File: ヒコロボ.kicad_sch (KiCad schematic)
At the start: 16 parts, among them U1 R3106GF, U2 4053, U3 4053, U5 R3106FG_IF

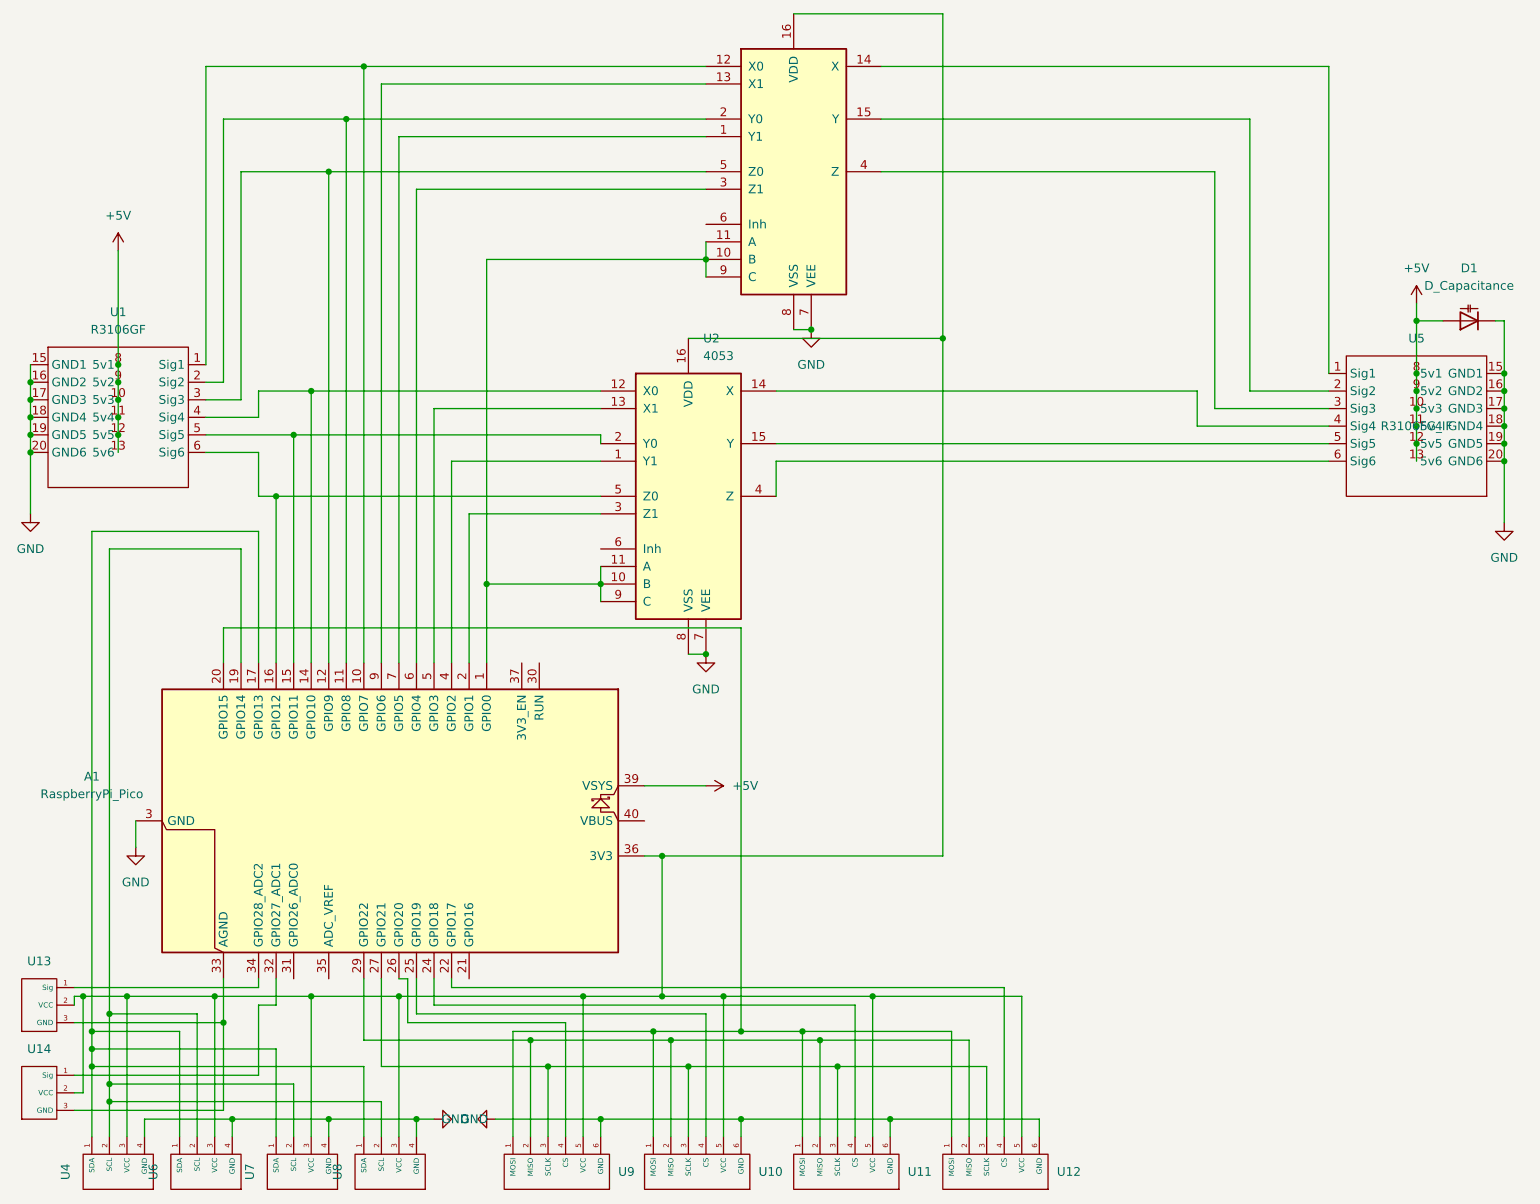
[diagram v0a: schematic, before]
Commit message: 基板回路を刷新
受信機をR3008SBに変更、Seeed XIAO追加、ラズパイ横に汎用ピン追加、各センサ用インターフェース追加
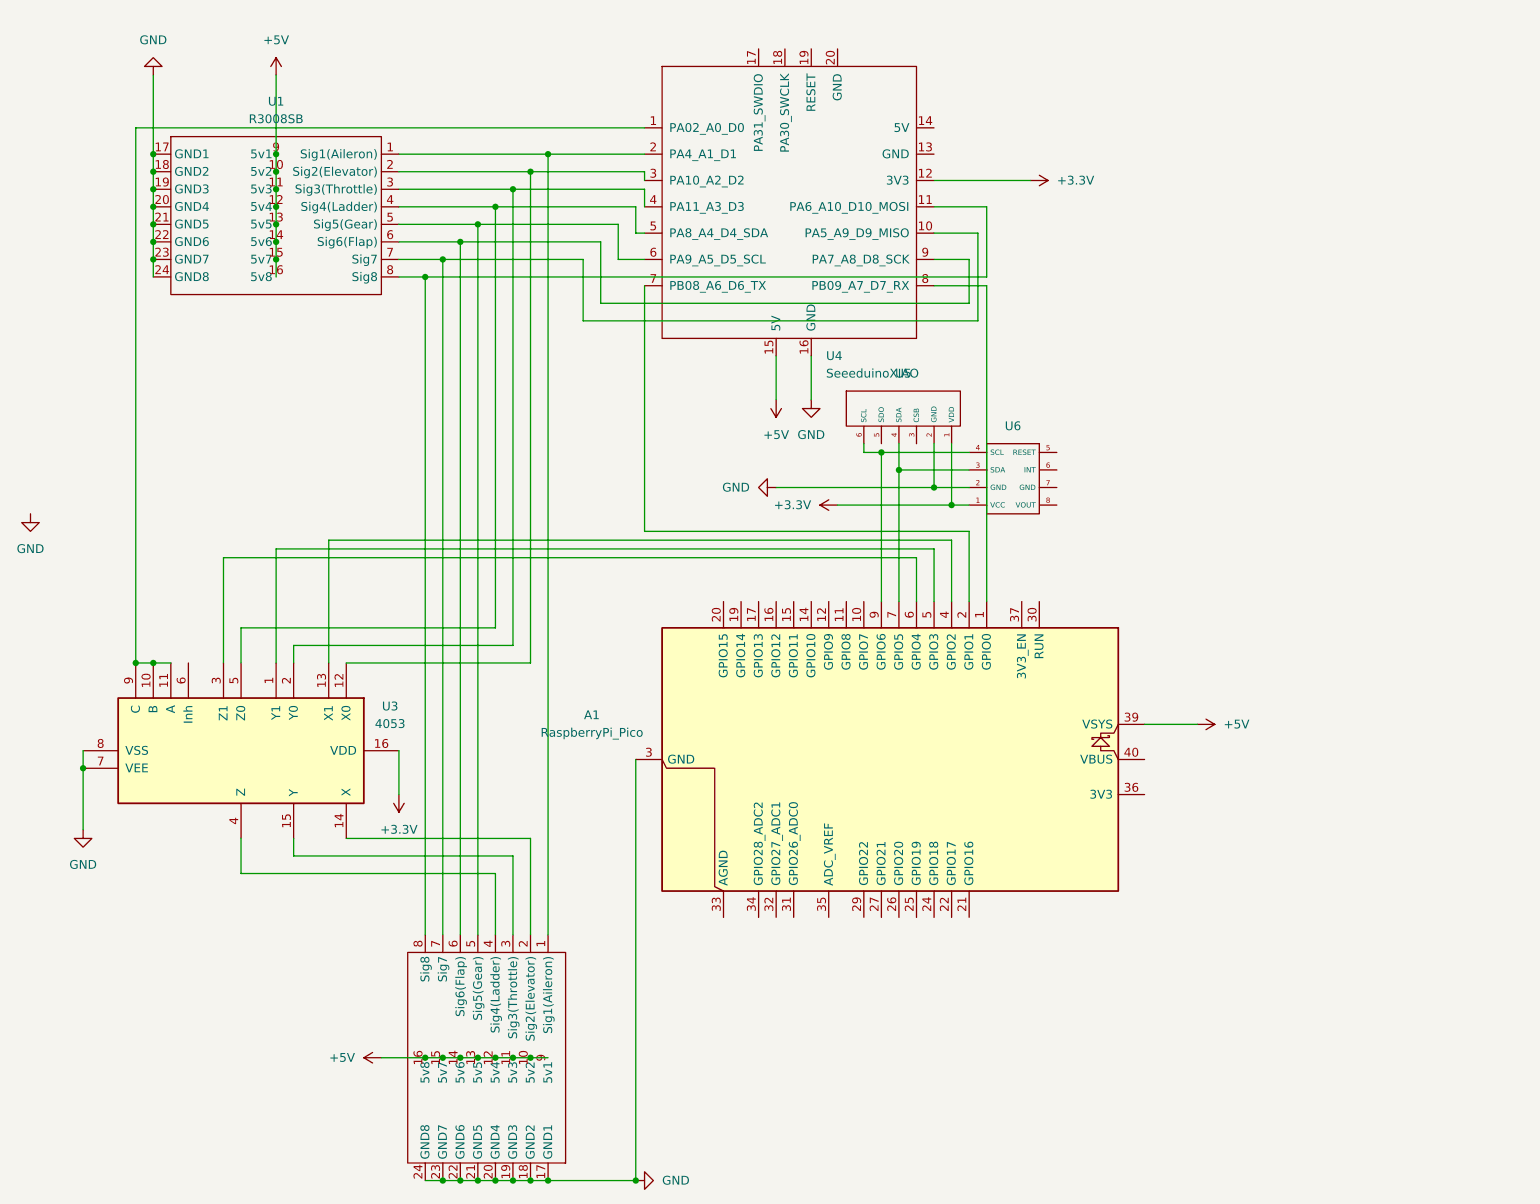
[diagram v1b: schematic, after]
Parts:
- removed D1: D_Capacitance, Capacitor_SMD:CP_Elec_8x10.5, symbol Device:D_Capacitance
- removed U1: R3106GF, Library:R3106FG, symbol My_Library:R3106GF
- removed U10, U11, U12, U9: (no value), Library:Sensor_SPI_IF, symbol My_Library:Sensor_SPI_IF
- removed U13, U14: (no value), Library:Sensor_Analog_IF, symbol My_Library:Sensor_Analog_IF
- removed U2: 4053, Library:DIP794W45P254L1969H508Q16, symbol 4xxx:4053
- removed U4, U6, U7, U8: (no value), Library:Sensor_I2C_IF, symbol My_Library:Sensor_IF
- removed U5: R3106FG_IF, Library:R3106FG, symbol My_Library:R3106GF_IF
- added U1: R3008SB, Library:R3008SB, symbol My_Library:R3008SB
- added U2: (no value), Library:R3008SB, symbol My_Library:R3008SB_IF
- added U4: SeeeduinoXIAO, Library:Seeeduino XIAO-MOUDLE14P-2.54-21X17.8MM, symbol My_Library:SeeeduinoXIAO
- added U5: (no value), Library:BMO280_IF, symbol My_Library:BME280_IF
- added U6: (no value), Library:BNO055_IF, symbol My_Library:BNE055_IF
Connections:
- net +5V: now also U1.10 (5v2), U1.11 (5v3), U1.12 (5v4), U1.13 (5v5), U1.14 (5v6), U1.15 (5v7), U1.16 (5v8), U1.9 (5v1), U2.10 (5v2), U2.11 (5v3), U2.12 (5v4), U2.13 (5v5), U2.14 (5v6), U2.15 (5v7), U2.16 (5v8), U2.9 (5v1), U4.15 (5V)
- net GND: now also U1.17 (GND1), U1.18 (GND2), U1.19 (GND3), U1.20 (GND4), U1.21 (GND5), U1.22 (GND6), U1.23 (GND7), U1.24 (GND8), U2.17 (GND1), U2.18 (GND2), U2.19 (GND3), U2.20 (GND4), U2.21 (GND5), U2.22 (GND6), U2.23 (GND7), U2.24 (GND8), U4.16 (GND), U5.2 (GND), U6.2 (GND)
- net at A1.7 (GPIO5): now also U5.4 (SDA), U6.3 (SDA); no longer U3.1 (Y1)
- net at U3.10 (B), U3.11 (A), U3.9 (C): now also U4.1 (PA02_A0_D0); no longer A1.1 (GPIO0)
- net at A1.10 (GPIO7): no longer U3.12 (X0)
- net at A1.9 (GPIO6): now also U5.6 (SCL), U6.4 (SCL); no longer U3.13 (X1)
- net at U3.14 (X): now also U2.2 (Sig2(Elevator))
- net at U3.15 (Y): now also U2.3 (Sig3(Throttle))
- net at A1.36 (3V3): no longer U3.16 (VDD)
- net at A1.11 (GPIO8): no longer U3.2 (Y0)
- net at U3.4 (Z): now also U2.4 (Sig4(Ladder))
- net at A1.12 (GPIO9): no longer U3.5 (Z0)
- net at A1.4 (GPIO2): now also U3.13 (X1)
- net at A1.5 (GPIO3): now also U3.1 (Y1)
- net at A1.2 (GPIO1): now also U4.7 (PB08_A6_D6_TX)
- new net: A1.1 (GPIO0), U4.8 (PB09_A7_D7_RX)
- new net: U1.1 (Sig1(Aileron)), U2.1 (Sig1(Aileron)), U4.2 (PA4_A1_D1)
- new net: U1.2 (Sig2(Elevator)), U3.12 (X0), U4.3 (PA10_A2_D2)
- new net: U1.3 (Sig3(Throttle)), U3.2 (Y0), U4.4 (PA11_A3_D3)
- new net: U1.4 (Sig4(Ladder)), U3.5 (Z0), U4.5 (PA8_A4_D4_SDA)
- new net: U1.5 (Sig5(Gear)), U2.5 (Sig5(Gear)), U4.6 (PA9_A5_D5_SCL)
- new net: U1.6 (Sig6(Flap)), U2.6 (Sig6(Flap)), U4.9 (PA7_A8_D8_SCK)
- new net: U1.7 (Sig7), U2.7 (Sig7), U4.10 (PA5_A9_D9_MISO)
- new net: U1.8 (Sig8), U2.8 (Sig8), U4.11 (PA6_A10_D10_MOSI)
- new net +3.3V: U3.16 (VDD), U4.12 (3V3), U5.1 (VDD), U6.1 (VCC)
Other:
- moved on the sheet: A1

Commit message: 確認お願いします。デザインルールチェッカーはエラーなしで通過してます。
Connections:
- net at U5.4 (SDA), U6.3 (SDA): now also A1.9 (GPIO6); no longer A1.7 (GPIO5)
- net at U5.6 (SCL), U6.4 (SCL): now also A1.10 (GPIO7); no longer A1.9 (GPIO6)
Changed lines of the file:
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@@
+	)
+	(junction
+		(at 139.7 82.55)
+		(diameter 0)
+		(color 0 0 0 0)
+	)
+	(junction
+		(at 134.62 80.01)
+		(diameter 0)
+		(color 0 0 0 0)
 	)
 	(junction
@@
 	)
 	(junction
-		(at 139.7 82.55)
-		(diameter 0)
-		(color 0 0 0 0)
-	)
-	(junction
 		(at 31.75 44.45)
 		(diameter 0)
@@
 	)
 	(junction
-		(at 137.16 80.01)
-		(diameter 0)
-		(color 0 0 0 0)
-	)
-	(junction
 		(at 49.53 36.83)
 		(diameter 0)
@@
 	(wire
 		(pts
-			(xy 137.16 80.01) (xy 134.62 80.01)
-		)
-		(stroke
-			(width 0)
-			(type default)
-		)
-	)
-	(wire
-		(pts
 			(xy 78.74 185.42) (xy 81.28 185.42)
 		)
@@
 	(wire
 		(pts
+			(xy 137.16 99.06) (xy 137.16 101.6)
+		)
+		(stroke
+			(width 0)
+			(type default)
+		)
+	)
+	(wire
+		(pts
 			(xy 182.88 119.38) (xy 175.26 119.38)
 		)
@@
 	(wire
 		(pts
-			(xy 137.16 101.6) (xy 137.16 80.01)
-		)
-		(stroke
-			(width 0)
-			(type default)
-		)
-	)
-	(wire
-		(pts
 			(xy 52.07 138.43) (xy 83.82 138.43)
 		)
@@
 	(wire
 		(pts
-			(xy 139.7 101.6) (xy 139.7 82.55)
-		)
-		(stroke
-			(width 0)
-			(type default)
-		)
-	)
-	(wire
-		(pts
 			(xy 73.66 52.07) (xy 93.98 52.07)
 		)
@@
 	(wire
 		(pts
+			(xy 139.7 82.55) (xy 139.7 99.06)
+		)
+		(stroke
+			(width 0)
+			(type default)
+		)
+	)
+	(wire
+		(pts
 			(xy 88.9 36.83) (xy 102.87 36.83)
 		)
@@
 	(wire
 		(pts
+			(xy 134.62 80.01) (xy 134.62 101.6)
+		)
+		(stroke
+			(width 0)
+			(type default)
+		)
+	)
+	(wire
+		(pts
 			(xy 67.31 36.83) (xy 88.9 36.83)
 		)
@@
 	(wire
 		(pts
-			(xy 149.86 80.01) (xy 137.16 80.01)
+			(xy 134.62 80.01) (xy 149.86 80.01)
 		)
 		(stroke
@@
 		)
 		(stroke
+			(width 0)
+			(type default)
+		)
+	)
+	(wire
+		(pts
+			(xy 139.7 99.06) (xy 137.16 99.06)
+		)
+		(stroke

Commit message: i2c周りの脆弱性修正
BNO055のi2c配線の修正、GNDピンの配線、電源ピン周りの配線などなど
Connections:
- net +3.3V: now also U5.3 (CSB)
- net +5V: now also U4.14 (5V)
- net GND: now also U4.13 (GND), U5.5 (SDO)

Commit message: 修正中
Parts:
- added J1: PINHD_1x2_Male, Connector_PinHeader_2.54mm:PinHeader_1x02_P2.54mm_Vertical, symbol PCM_SL_Pin_Headers:PINHD_1x2_Male
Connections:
- net +3.3V: now also A1.36 (3V3); no longer U4.12 (3V3)
- net at A1.20 (GPIO15): now also J1.2
- net at U3.10 (B), U3.11 (A), U3.9 (C)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: now also J1.1
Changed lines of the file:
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@@
 	)
 	(junction
+		(at 29.21 81.28)
+		(diameter 0)
+		(color 0 0 0 0)
+	)
+	(junction
 		(at 49.53 49.53)
 		(diameter 0)
@@
 	(wire
 		(pts
+			(xy 114.3 99.06) (xy 114.3 101.6)
+		)
+		(stroke
+			(width 0)
+			(type default)
+		)
+	)
+	(wire
+		(pts
 			(xy 49.53 44.45) (xy 49.53 46.99)
 		)
@@
 	(wire
 		(pts
-			(xy 29.21 110.49) (xy 29.21 33.02)
+			(xy 29.21 110.49) (xy 29.21 81.28)
 		)
 		(stroke
@@
 	(wire
 		(pts
-			(xy 158.75 40.64) (xy 144.78 40.64)
-		)
-		(stroke
-			(width 0)
-			(type default)
-		)
-	)
-	(wire
-		(pts
 			(xy 88.9 185.42) (xy 101.6 185.42)
 		)
@@
 	(wire
 		(pts
+			(xy 175.26 129.54) (xy 180.34 129.54)
+		)
+		(stroke
+			(width 0)
+			(type default)
+		)
+	)
+	(wire
+		(pts
 			(xy 88.9 149.86) (xy 88.9 36.83)
 		)
@@
 	(wire
 		(pts
+			(xy 92.71 99.06) (xy 114.3 99.06)
+		)
+		(stroke
+			(width 0)
+			(type default)
+		)
+	)
+	(wire
+		(pts
 			(xy 29.21 110.49) (xy 31.75 110.49)
 		)
@@
 	(wire
 		(pts
+			(xy 92.71 83.82) (xy 92.71 99.06)
+		)
+		(stroke
+			(width 0)
+			(type default)
+		)
+	)
+	(wire
+		(pts
 			(xy 81.28 167.64) (xy 83.82 167.64)
 		)
@@
 	(wire
 		(pts
+			(xy 29.21 81.28) (xy 92.71 81.28)
+		)
+		(stroke
+			(width 0)
+			(type default)
+		)
+	)
+	(wire
+		(pts
 			(xy 81.28 140.97) (xy 81.28 149.86)
 		)
@@
 	(wire
 		(pts
+			(xy 29.21 81.28) (xy 29.21 33.02)
+		)
+		(stroke
+			(width 0)
+			(type default)
+		)
+	)
+	(wire
+		(pts
 			(xy 139.7 99.06) (xy 137.16 99.06)
 		)
@@
 	)
 	(symbol
-		(lib_id "power:+3.3V")
-		(at 158.75 40.64 270)
-		(unit 1)
-		(body_style 1)
-		(exclude_from_sim no)
-		(in_bom yes)
-		(on_board yes)
-		(in_pos_files yes)
-		(dnp no)
-		(fields_autoplaced yes)
-		(property "Reference" "#PWR07"
-			(at 154.94 40.64 0)
-			(hide yes)
-			(show_name no)
-			(do_not_autoplace no)
-			(effects
-				(font
-					(size 1.27 1.27)
-				)
-			)
-		)
-		(property "Value" "+3.3V"
-			(at 162.56 40.6399 90)
-			(show_name no)
-			(do_not_autoplace no)
-			(effects
-				(font
-					(size 1.27 1.27)
-				)
-				(justify left)
-			)
-		)
-		(property "Footprint" ""
-			(at 158.75 40.64 0)
-			(hide yes)
-			(show_name no)
-			(do_not_autoplace no)
-			(effects
-				(font
-					(size 1.27 1.27)
-				)
-			)
-		)
-		(property "Datasheet" ""
-			(at 158.75 40.64 0)
-			(hide yes)
-			(show_name no)
-			(do_not_autoplace no)
-			(effects
-				(font
-					(size 1.27 1.27)
-				)
-			)
-		)
-		(property "Description" "Power symbol creates a global label with name \"+3.3V\""
-			(at 158.75 40.64 0)
-			(hide yes)
-			(show_name no)
-			(do_not_autoplace no)
-			(effects
-				(font
-					(size 1.27 1.27)
-				)
-			)
-		)
-		(pin "1"
-		)
-		(instances
-			(project "ヒコロボ"
-				(path "/ff0925a6-2969-4ba9-b4fe-9000bc3f53f1"
-					(reference "#PWR07")
-					(unit 1)
-				)
-			)
-		)
-	)
-	(symbol
 		(lib_id "power:+5V")
 		(at 151.13 33.02 270)
@@
 	)
 	(symbol
+		(lib_id "PCM_SL_Pin_Headers:PINHD_1x2_Male")
+		(at 96.52 82.55 0)
+		(unit 1)
+		(body_style 1)
+		(exclude_from_sim no)
+		(in_bom yes)
+		(on_board yes)
+		(in_pos_files yes)
+		(dnp no)
+		(fields_autoplaced yes)
+		(property "Reference" "J1"
+			(at 99.06 81.2799 0)
+			(show_name no)
+			(do_not_autoplace no)
+			(effects
+				(font
+					(size 1.27 1.27)
+				)
+				(justify left)
+			)
+		)
+		(property "Value" "PINHD_1x2_Male"
+			(at 99.06 83.8199 0)
+			(show_name no)
+			(do_not_autoplace no)
+			(effects
+				(font
+					(size 1.27 1.27)
+				)
+				(justify left)
+			)
+		)
+		(property "Footprint" "Connector_PinHeader_2.54mm:PinHeader_1x02_P2.54mm_Vertical"
+			(at 97.79 86.36 0)
+			(hide yes)
+			(show_name no)
+			(do_not_autoplace no)
+			(effects
+				(font
+					(size 1.27 1.27)
+				)
+			)
+		)
+		(property "Datasheet" ""
+			(at 96.52 74.93 0)
+			(hide yes)
+			(show_name no)
+			(do_not_autoplace no)
+			(effects
+				(font
+					(size 1.27 1.27)
+				)
+			)
+		)
+		(property "Description" "Pin Header male with pin space 2.54mm. Pin Count -2"
+			(at 96.52 82.55 0)
+			(hide yes)
+			(show_name no)
+			(do_not_autoplace no)
+			(effects
+				(font
+					(size 1.27 1.27)
+				)
+			)
+		)
+		(pin "1"
+		)
+		(pin "2"
+		)
+		(instances
+			(project "ヒコロボ"
+				(path "/ff0925a6-2969-4ba9-b4fe-9000bc3f53f1"
+					(reference "J1")
+					(unit 1)
+				)
+			)
+		)
+	)
+	(symbol
 		(lib_id "power:GND")
 		(at 101.6 185.42 90)
@@
 					(unit 1)
 				)
+			)
+		)
+	)
+	(symbol
+		(lib_id "power:+3.3V")
+		(at 180.34 129.54 270)
+		(unit 1)
+		(body_style 1)
+		(exclude_from_sim no)
+		(in_bom yes)
+		(on_board yes)
+		(in_pos_files yes)
+		(dnp no)
+		(fields_autoplaced yes)
+		(property "Reference" "#PWR07"
+			(at 176.53 129.54 0)
+			(hide yes)
+			(show_name no)
+			(do_not_autoplace no)
+			(effects
+				(font
+					(size 1.27 1.27)
+				)
+			)
+		)
+		(property "Value" "+3.3V"
+			(at 184.15 129.5399 90)
+			(show_name no)
+			(do_not_autoplace no)
+			(effects
+				(font
+					(size 1.27 1.27)
+				)
+				(justify left)
+			)
+		)
+		(property "Footprint" ""
+			(at 180.34 129.54 0)
+			(hide yes)
+			(show_name no)
+			(do_not_autoplace no)
+			(effects
+				(font
+					(size 1.27 1.27)
+				)
+			)
+		)
+		(property "Datasheet" ""
+			(at 180.34 129.54 0)
+			(hide yes)
+			(show_name no)
+			(do_not_autoplace no)
+			(effects
+				(font
+					(size 1.27 1.27)
+				)
+			)
+		)
+		(property "Description" "Power symbol creates a global label with name \"+3.3V\""
+			(at 180.34 129.54 0)
+			(hide yes)
+			(show_name no)
+			(do_not_autoplace no)
+			(effects
+				(font
+					(size 1.27 1.27)
+				)
+			)
+		)
+		(pin "1"
+		)
+		(instances
+			(project "ヒコロボ"
+				(path "/ff0925a6-2969-4ba9-b4fe-9000bc3f53f1"
+					(reference "#PWR07")
+					(unit 1)
+				)

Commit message: 完成
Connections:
- net +5V: no longer U4.15 (5V)
- net GND: now also U3.6 (Inh); no longer U4.16 (GND)
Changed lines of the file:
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@@
 	)
 	(junction
+		(at 21.59 123.19)
+		(diameter 0)
+		(color 0 0 0 0)
+	)
+	(junction
 		(at 81.28 44.45)
 		(diameter 0)
@@
 	(wire
 		(pts
+			(xy 36.83 107.95) (xy 36.83 110.49)
+		)
+		(stroke
+			(width 0)
+			(type default)
+		)
+	)
+	(wire
+		(pts
 			(xy 142.24 101.6) (xy 142.24 95.25)
 		)
@@
 	(wire
 		(pts
-			(xy 21.59 123.19) (xy 21.59 125.73)
+			(xy 21.59 107.95) (xy 21.59 123.19)
 		)
 		(stroke
@@
 	(wire
 		(pts
-			(xy 88.9 185.42) (xy 101.6 185.42)
+			(xy 21.59 123.19) (xy 21.59 125.73)
 		)
 		(stroke
@@
 	(wire
 		(pts
-			(xy 121.92 66.04) (xy 121.92 72.39)
+			(xy 88.9 185.42) (xy 101.6 185.42)
 		)
 		(stroke
@@
 	(wire
 		(pts
+			(xy 21.59 107.95) (xy 36.83 107.95)
+		)
+		(stroke
+			(width 0)
+			(type default)
+		)
+	)
+	(wire
+		(pts
 			(xy 147.32 101.6) (xy 147.32 92.71)
 		)
@@
 	(wire
 		(pts
-			(xy 127 72.39) (xy 127 66.04)
-		)
-		(stroke
-			(width 0)
-			(type default)
-		)
-	)
-	(wire
-		(pts
 			(xy 76.2 167.64) (xy 78.74 167.64)
 		)
@@
 	(symbol
 		(lib_id "power:GND")
-		(at 127 72.39 0)
-		(unit 1)
-		(body_style 1)
-		(exclude_from_sim no)
-		(in_bom yes)
-		(on_board yes)
-		(in_pos_files yes)
-		(dnp no)
-		(fields_autoplaced yes)
-		(property "Reference" "#PWR04"
-			(at 127 78.74 0)
-			(hide yes)
-			(show_name no)
-			(do_not_autoplace no)
-			(effects
-				(font
-					(size 1.27 1.27)
-				)
-			)
-		)
-		(property "Value" "GND"
-			(at 127 77.47 0)
-			(show_name no)
-			(do_not_autoplace no)
-			(effects
-				(font
-					(size 1.27 1.27)
-				)
-			)
-		)
-		(property "Footprint" ""
-			(at 127 72.39 0)
-			(hide yes)
-			(show_name no)
-			(do_not_autoplace no)
-			(effects
-				(font
-					(size 1.27 1.27)
-				)
-			)
-		)
-		(property "Datasheet" ""
-			(at 127 72.39 0)
-			(hide yes)
-			(show_name no)
-			(do_not_autoplace no)
-			(effects
-				(font
-					(size 1.27 1.27)
-				)
-			)
-		)
-		(property "Description" "Power symbol creates a global label with name \"GND\" , ground"
-			(at 127 72.39 0)
-			(hide yes)
-			(show_name no)
-			(do_not_autoplace no)
-			(effects
-				(font
-					(size 1.27 1.27)
-				)
-			)
-		)
-		(pin "1"
-		)
-		(instances
-			(project "ヒコロボ"
-				(path "/ff0925a6-2969-4ba9-b4fe-9000bc3f53f1"
-					(reference "#PWR04")
-					(unit 1)
-				)
-			)
-		)
-	)
-	(symbol
-		(lib_id "power:GND")
 		(at 21.59 134.62 0)
 		(unit 1)
@@
 					(unit 1)
 				)
-			)
-		)
-	)
-	(symbol
-		(lib_id "power:+5V")
-		(at 121.92 72.39 180)
-		(unit 1)
-		(body_style 1)
-		(exclude_from_sim no)
-		(in_bom yes)
-		(on_board yes)
-		(in_pos_files yes)
-		(dnp no)
-		(fields_autoplaced yes)
-		(property "Reference" "#PWR02"
-			(at 121.92 68.58 0)
-			(hide yes)
-			(show_name no)
-			(do_not_autoplace no)
-			(effects
-				(font
-					(size 1.27 1.27)
-				)
-			)
-		)
-		(property "Value" "+5V"
-			(at 121.92 77.47 0)
-			(show_name no)
-			(do_not_autoplace no)
-			(effects
-				(font
-					(size 1.27 1.27)
-				)
-			)
-		)
-		(property "Footprint" ""
-			(at 121.92 72.39 0)
-			(hide yes)
-			(show_name no)
-			(do_not_autoplace no)
-			(effects
-				(font
-					(size 1.27 1.27)
-				)
-			)
-		)
-		(property "Datasheet" ""
-			(at 121.92 72.39 0)
-			(hide yes)
-			(show_name no)
-			(do_not_autoplace no)
-			(effects
-				(font
-					(size 1.27 1.27)
-				)
-			)
-		)
-		(property "Description" "Power symbol creates a global label with name \"+5V\""
-			(at 121.92 72.39 0)
-			(hide yes)
-			(show_name no)
-			(do_not_autoplace no)
-			(effects
-				(font
-					(size 1.27 1.27)
-				)
-			)
-		)
-		(pin "1"
-		)
-		(instances
-			(project "ヒコロボ"
-				(path "/ff0925a6-2969-4ba9-b4fe-9000bc3f53f1"
-					(reference "#PWR02")
-					(unit 1)
-				)
